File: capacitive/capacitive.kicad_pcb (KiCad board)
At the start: 2 copper layers, 78 x 72 mm, 84 parts, among them J101 UL, J102 UART, J103 SWD, J104 TX_PADS, J105 RX_PAD, J106 POWER, J107 UR, J108 LL, J109 LR, Q101 RU1C002ZPTCL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

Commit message: Move capacitor so it doesn't cover some designators
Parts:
- moved R121 9.40 mm to (139.8, 102.9), turned to 180 degrees
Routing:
- net Net-(C124-Pad2): track 21.2 -> 28.6 mm
- net Net-(C126-Pad2): track 17.1 -> 12.3 mm
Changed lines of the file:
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@@
   )
   (setup
-    (last_trace_width 0.3)
+    (last_trace_width 0.45)
     (user_trace_width 0.2)
     (user_trace_width 0.3)
@@
     (tags "resistor 1206")
     (attr smd)
-    (fp_text reference R117 (at 0.21 9.035 270) (layer F.SilkS)
+    (fp_text reference R117 (at 0.21 7.225 270) (layer F.SilkS)
       (effects (font (size 1 1) (thickness 0.15)))
     )
@@
     (tags "resistor 1206")
     (attr smd)
-    (fp_text reference R127 (at 0.195 10.125 270) (layer F.SilkS)
+    (fp_text reference R127 (at 0.195 8.495 270) (layer F.SilkS)
       (effects (font (size 1 1) (thickness 0.15)))
     )
@@
   )
   (module Resistors_SMD:R_1206_HandSoldering (layer F.Cu)
-    (at 143.51 94.24 270)
+    (at 139.795 102.87 180)
     (descr "Resistor SMD 1206, hand soldering")
     (tags "resistor 1206")
     (attr smd)
-    (fp_text reference R121 (at 0 -1.85 270) (layer F.SilkS)
+    (fp_text reference R121 (at 0 -1.85 180) (layer F.SilkS)
       (effects (font (size 1 1) (thickness 0.15)))
     )
-    (fp_text value "100k 1%" (at 0 1.9 270) (layer F.Fab)
+    (fp_text value "100k 1%" (at 0 1.9 180) (layer F.Fab)
       (effects (font (size 1 1) (thickness 0.15)))
     )
@@
     (fp_line (start 1.6 0.8) (end -1.6 0.8) (layer F.Fab) (width 0.1))
     (fp_line (start -1.6 0.8) (end -1.6 -0.8) (layer F.Fab) (width 0.1))
-    (fp_text user %R (at 0 0 270) (layer F.Fab)
+    (fp_text user %R (at 0 0 180) (layer F.Fab)
       (effects (font (size 0.7 0.7) (thickness 0.105)))
     )
-    (pad 2 smd rect (at 2 0 270) (size 2 1.7) (layers F.Cu F.Paste F.Mask)
+    (pad 2 smd rect (at 2 0 180) (size 2 1.7) (layers F.Cu F.Paste F.Mask)
       (net 37 "Net-(C126-Pad2)"))
-    (pad 1 smd rect (at -2 0 270) (size 2 1.7) (layers F.Cu F.Paste F.Mask)
+    (pad 1 smd rect (at -2 0 180) (size 2 1.7) (layers F.Cu F.Paste F.Mask)
       (net 34 "Net-(C124-Pad2)"))
     (model ${KISYS3DMOD}/Resistors_SMD.3dshapes/R_1206.wrl
@@
   (segment (start 133.18 93.13) (end 132.48 92.43) (width 0.3) (layer B.Cu) (net 34))
   (via (at 132.48 92.43) (size 0.6858) (drill 0.3302) (layers F.Cu B.Cu) (net 34))
-  (segment (start 141.125 92.24) (end 140.41 92.955) (width 0.3) (layer F.Cu) (net 34))
   (segment (start 140.41 92.955) (end 140.41 93.18) (width 0.3) (layer F.Cu) (net 34))
-  (segment (start 143.51 92.24) (end 141.125 92.24) (width 0.3) (layer F.Cu) (net 34))
+  (segment (start 141.795 101.57) (end 141.795 102.87) (width 0.45) (layer F.Cu) (net 34))
+  (segment (start 141.795 93.74) (end 141.795 101.57) (width 0.45) (layer F.Cu) (net 34))
+  (segment (start 141.235 93.18) (end 141.795 93.74) (width 0.45) (layer F.Cu) (net 34))
+  (segment (start 140.41 93.18) (end 141.235 93.18) (width 0.45) (layer F.Cu) (net 34))
   (segment (start 138.05 89.54) (end 138.05 87.69) (width 0.6) (layer F.Cu) (net 35))
   (segment (start 138.05 87.69) (end 138.05 85.695678) (width 0.6) (layer F.Cu) (net 35))
@@
   (segment (start 132.334952 95.69) (end 131.3 95.69) (width 0.3) (layer F.Cu) (net 37))
   (segment (start 132.650254 96.005302) (end 132.334952 95.69) (width 0.3) (layer F.Cu) (net 37))
-  (segment (start 135.312401 99.302401) (end 135.04 99.03) (width 0.3) (layer F.Cu) (net 37))
-  (segment (start 135.04 99.03) (end 134.14 99.03) (width 0.3) (layer F.Cu) (net 37))
-  (segment (start 140.597599 99.302401) (end 135.312401 99.302401) (width 0.3) (layer F.Cu) (net 37))
-  (segment (start 143.51 96.39) (end 140.597599 99.302401) (width 0.3) (layer F.Cu) (net 37))
-  (segment (start 143.51 96.24) (end 143.51 96.39) (width 0.3) (layer F.Cu) (net 37))
+  (segment (start 137.795 101.57) (end 137.795 102.87) (width 0.45) (layer F.Cu) (net 37))
+  (segment (start 135.255 99.03) (end 137.795 101.57) (width 0.45) (layer F.Cu) (net 37))
+  (segment (start 134.14 99.03) (end 135.255 99.03) (width 0.45) (layer F.Cu) (net 37))
   (segment (start 133.945 100.42) (end 134.17 100.42) (width 0.2) (layer F.Cu) (net 38))
   (segment (start 132.83 97.66) (end 132.83 98.16) (width 0.2) (layer F.Cu) (net 38))

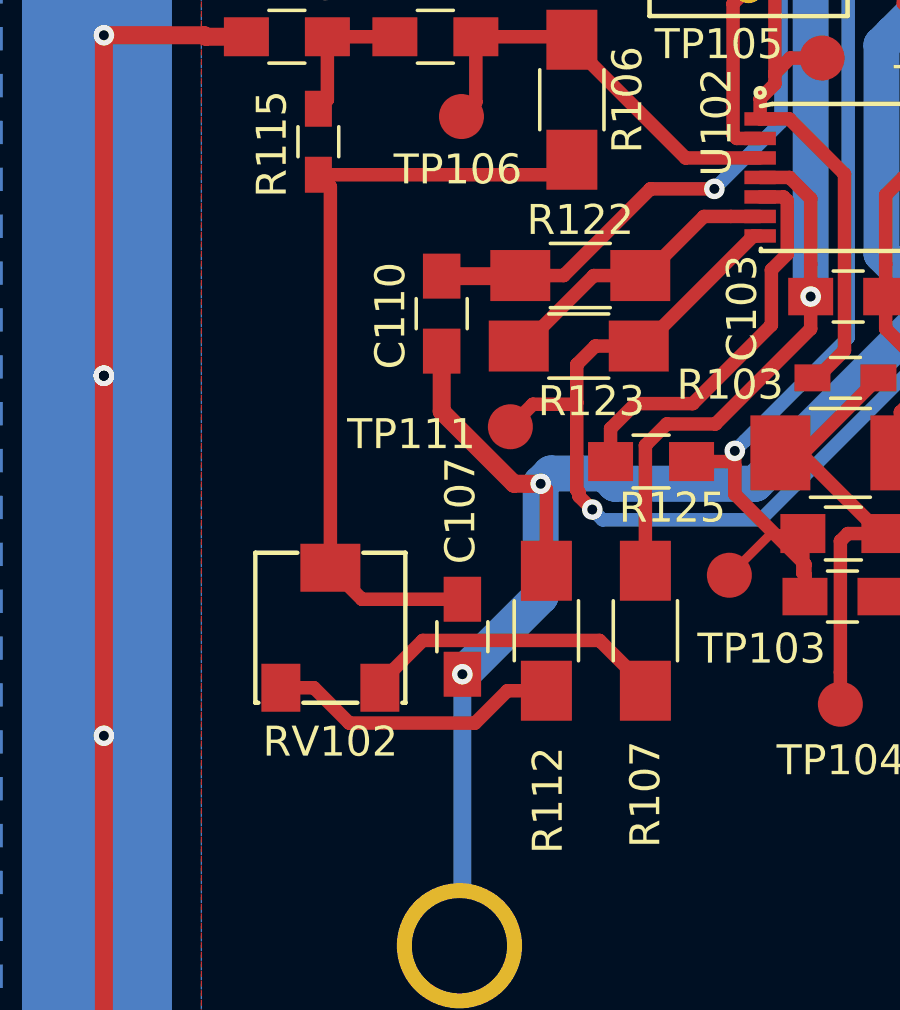
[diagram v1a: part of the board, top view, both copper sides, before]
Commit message: Flip offset pot around to make it more accessible TODO maybe remove offset pot to save cost
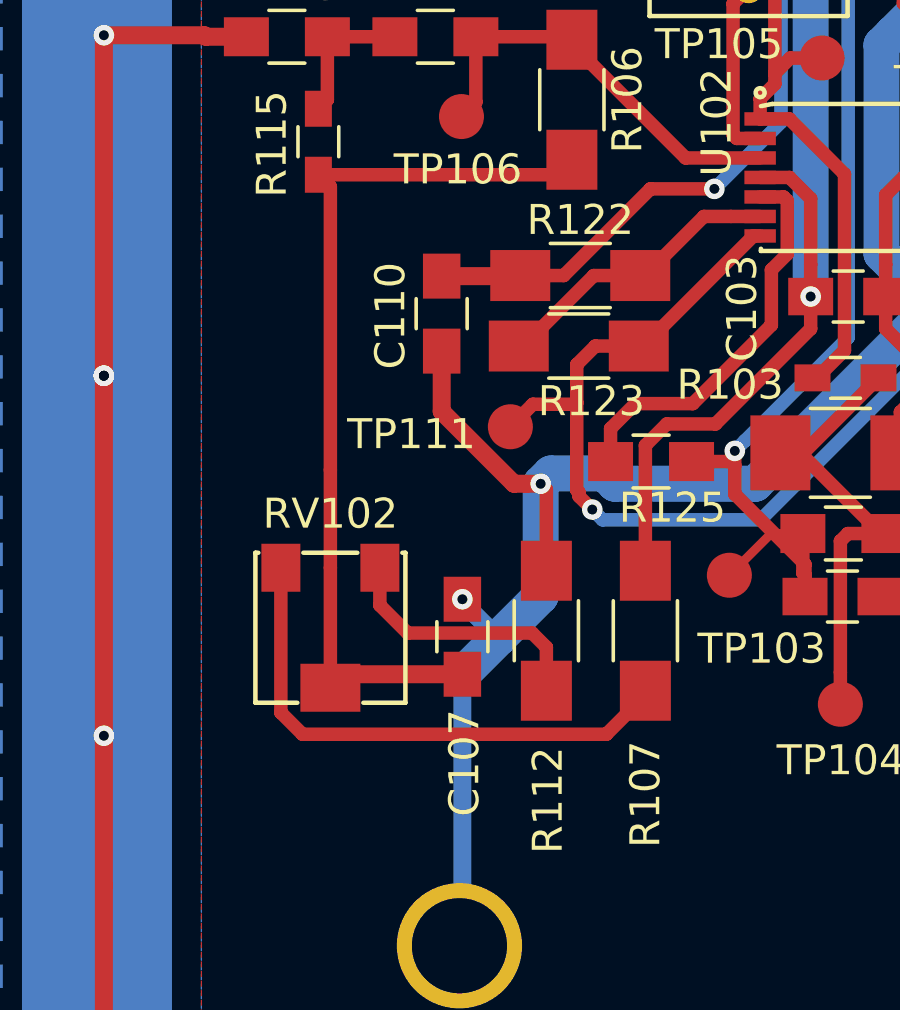
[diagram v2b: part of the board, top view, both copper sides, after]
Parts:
- turned C107 to 90 degrees
- turned RV102 to 180 degrees
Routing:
- net Net-(R107-Pad2): track 10.4 -> 18.1 mm
- net Net-(C107-Pad1): track 26.8 -> 30.5 mm
- net GND: track 430.9 -> 432.7 mm
- net Net-(R112-Pad1): track 9.78 -> 8.83 mm
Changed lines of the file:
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@@
     (thickness 1.6)
     (drawings 9)
-    (tracks 810)
+    (tracks 816)
     (zones 0)
     (modules 84)
@@
   )
   (setup
-    (last_trace_width 0.45)
+    (last_trace_width 0.6)
     (user_trace_width 0.2)
     (user_trace_width 0.3)
@@
   )
   (module capacitive:Bourns-PVG5H (layer F.Cu)
-    (at 110.6 109.4)
-    (fp_text reference RV102 (at 0 3.8) (layer F.SilkS)
+    (at 110.6 109.4 180)
+    (fp_text reference RV102 (at 0 3.8 180) (layer F.SilkS)
       (effects (font (size 1 1) (thickness 0.15)))
     )
-    (fp_text value "5k linear" (at 0 -3.7) (layer F.Fab)
+    (fp_text value "5k linear" (at 0 -3.7 180) (layer F.Fab)
       (effects (font (size 1 1) (thickness 0.15)))
     )
@@
     (fp_line (start -2.5 -2.5) (end -2.5 2.5) (layer F.SilkS) (width 0.15))
     (fp_line (start -1.1 -2.5) (end -2.5 -2.5) (layer F.SilkS) (width 0.15))
-    (pad 2 smd rect (at 0 -2) (size 2 1.6) (layers F.Cu F.Paste F.Mask)
+    (pad 2 smd rect (at 0 -2 180) (size 2 1.6) (layers F.Cu F.Paste F.Mask)
       (net 31 "Net-(C107-Pad1)"))
-    (pad 1 smd rect (at 1.65 2) (size 1.3 1.6) (layers F.Cu F.Paste F.Mask)
+    (pad 1 smd rect (at 1.65 2 180) (size 1.3 1.6) (layers F.Cu F.Paste F.Mask)
       (net 29 "Net-(R107-Pad2)"))
-    (pad 3 smd rect (at -1.65 2) (size 1.3 1.6) (layers F.Cu F.Paste F.Mask)
+    (pad 3 smd rect (at -1.65 2 180) (size 1.3 1.6) (layers F.Cu F.Paste F.Mask)
       (net 30 "Net-(R112-Pad1)"))
   )
@@
   )
   (module Capacitors_SMD:C_0805_HandSoldering (layer F.Cu)
-    (at 115 109.7 270)
+    (at 115 109.7 90)
     (descr "Capacitor SMD 0805, hand soldering")
     (tags "capacitor 0805")
     (attr smd)
-    (fp_text reference C107 (at -4.20624 0.06604 270) (layer F.SilkS)
+    (fp_text reference C107 (at -4.20624 0.06604 90) (layer F.SilkS)
       (effects (font (size 1 1) (thickness 0.15)))
     )
-    (fp_text value "100nF 20%" (at 0 1.75 270) (layer F.Fab)
+    (fp_text value "100nF 20%" (at 0 1.75 90) (layer F.Fab)
       (effects (font (size 1 1) (thickness 0.15)))
     )
-    (fp_text user %R (at 0 -1.75 270) (layer F.Fab)
+    (fp_text user %R (at 0 -1.75 90) (layer F.Fab)
       (effects (font (size 1 1) (thickness 0.15)))
     )
@@
     (fp_line (start 2.25 0.87) (end 2.25 -0.88) (layer F.CrtYd) (width 0.05))
     (fp_line (start 2.25 0.87) (end -2.25 0.87) (layer F.CrtYd) (width 0.05))
-    (pad 1 smd rect (at -1.25 0 270) (size 1.5 1.25) (layers F.Cu F.Paste F.Mask)
+    (pad 1 smd rect (at -1.25 0 90) (size 1.5 1.25) (layers F.Cu F.Paste F.Mask)
       (net 31 "Net-(C107-Pad1)"))
-    (pad 2 smd rect (at 1.25 0 270) (size 1.5 1.25) (layers F.Cu F.Paste F.Mask)
+    (pad 2 smd rect (at 1.25 0 90) (size 1.5 1.25) (layers F.Cu F.Paste F.Mask)
       (net 2 GND))
     (model Capacitors_SMD.3dshapes/C_0805.wrl
@@
   (via (at 130.73 88.21) (size 0.6858) (drill 0.3302) (layers F.Cu B.Cu) (net 2))
   (segment (start 117.61 104.6) (end 117.61 108.34) (width 1.2) (layer B.Cu) (net 2))
-  (segment (start 117.61 108.34) (end 115 110.95) (width 1.2) (layer B.Cu) (net 2))
   (segment (start 129.11 98.36) (end 130.4 98.36) (width 0.6) (layer F.Cu) (net 2))
   (segment (start 130.4 98.36) (end 130.47 98.43) (width 0.6) (layer F.Cu) (net 2))
@@
   (segment (start 130.4 61.125) (end 130.4 61) (width 0.6) (layer F.Cu) (net 2))
   (segment (start 135.95 62.47) (end 137.02 62.47) (width 0.6) (layer F.Cu) (net 2))
-  (via (at 115 110.95) (size 0.6858) (drill 0.3302) (layers F.Cu B.Cu) (net 2))
   (segment (start 117.8 107.5) (end 117.8 104.79) (width 0.45) (layer F.Cu) (net 2))
   (segment (start 117.8 104.79) (end 117.61 104.6) (width 0.45) (layer F.Cu) (net 2))
@@
   (segment (start 118.33 63.05) (end 119.26 63.98) (width 0.6) (layer F.Cu) (net 2))
   (segment (start 119.26 63.98) (end 123.74 63.98) (width 0.6) (layer F.Cu) (net 2))
+  (via (at 115 108.45) (size 0.6858) (drill 0.3302) (layers F.Cu B.Cu) (net 2))
+  (segment (start 115 108.45) (end 115 108.54) (width 0.6) (layer B.Cu) (net 2))
+  (segment (start 117.61 108.34) (end 116.205 109.745) (width 1.2) (layer B.Cu) (net 2))
+  (segment (start 115 108.54) (end 116.205 109.745) (width 0.6) (layer B.Cu) (net 2))
+  (segment (start 116.205 109.745) (end 115 110.95) (width 1.2) (layer B.Cu) (net 2))
   (segment (start 136.28 70.15) (end 134.65 70.15) (width 0.45) (layer F.Cu) (net 3))
   (segment (start 134.65 70.15) (end 132.9 68.4) (width 0.45) (layer F.Cu) (net 3))
@@
   (segment (start 90.649999 68.949999) (end 89.9 68.2) (width 0.3) (layer F.Cu) (net 28))
   (segment (start 121.1 111.5) (end 121.1 111.35) (width 0.45) (layer F.Cu) (net 29))
-  (segment (start 121.1 111.35) (end 119.572599 109.822599) (width 0.45) (layer F.Cu) (net 29))
-  (segment (start 119.572599 109.822599) (end 113.677401 109.822599) (width 0.45) (layer F.Cu) (net 29))
-  (segment (start 113.677401 109.822599) (end 112.25 111.25) (width 0.45) (layer F.Cu) (net 29))
-  (segment (start 112.25 111.25) (end 112.25 111.4) (width 0.45) (layer F.Cu) (net 29))
-  (segment (start 117.8 111.5) (end 116.5 111.5) (width 0.45) (layer F.Cu) (net 30))
-  (segment (start 116.5 111.5) (end 115.422599 112.577401) (width 0.45) (layer F.Cu) (net 30))
-  (segment (start 115.422599 112.577401) (end 111.227401 112.577401) (width 0.45) (layer F.Cu) (net 30))
-  (segment (start 111.227401 112.577401) (end 110.05 111.4) (width 0.45) (layer F.Cu) (net 30))
-  (segment (start 110.05 111.4) (end 108.95 111.4) (width 0.45) (layer F.Cu) (net 30))
+  (segment (start 119.8 112.95) (end 121.1 111.65) (width 0.45) (layer F.Cu) (net 29))
+  (segment (start 109.670678 112.95) (end 119.8 112.95) (width 0.45) (layer F.Cu) (net 29))
+  (segment (start 108.95 112.229322) (end 109.670678 112.95) (width 0.45) (layer F.Cu) (net 29))
+  (segment (start 121.1 111.65) (end 121.1 111.5) (width 0.45) (layer F.Cu) (net 29))
+  (segment (start 108.95 107.4) (end 108.95 112.229322) (width 0.45) (layer F.Cu) (net 29))
+  (segment (start 112.25 108.65) (end 112.25 107.4) (width 0.45) (layer F.Cu) (net 30))
+  (segment (start 117.327401 109.577401) (end 113.177401 109.577401) (width 0.45) (layer F.Cu) (net 30))
+  (segment (start 117.8 110.05) (end 117.327401 109.577401) (width 0.45) (layer F.Cu) (net 30))
+  (segment (start 113.177401 109.577401) (end 112.25 108.65) (width 0.45) (layer F.Cu) (net 30))
+  (segment (start 117.8 111.5) (end 117.8 110.05) (width 0.45) (layer F.Cu) (net 30))
   (segment (start 110.2 94.3) (end 118.15 94.3) (width 0.45) (layer F.Cu) (net 31))
   (segment (start 118.15 94.3) (end 118.65 93.8) (width 0.45) (layer F.Cu) (net 31))
-  (segment (start 110.6 107.4) (end 110.6 94.7) (width 0.45) (layer F.Cu) (net 31))
   (segment (start 110.6 94.7) (end 110.2 94.3) (width 0.45) (layer F.Cu) (net 31))
-  (segment (start 115 108.45) (end 111.65 108.45) (width 0.45) (layer F.Cu) (net 31))
-  (segment (start 111.65 108.45) (end 110.6 107.4) (width 0.45) (layer F.Cu) (net 31))
+  (segment (start 110.6 107.4) (end 110.6 104.14) (width 0.45) (layer F.Cu) (net 31))
+  (segment (start 110.6 104.14) (end 110.6 94.7) (width 0.45) (layer F.Cu) (net 31))
+  (segment (start 110.6 107.4) (end 110.6 111.4) (width 0.45) (layer F.Cu) (net 31))
+  (segment (start 111.05 110.95) (end 110.6 111.4) (width 0.6) (layer F.Cu) (net 31))
+  (segment (start 115 110.95) (end 111.05 110.95) (width 0.6) (layer F.Cu) (net 31))
   (segment (start 123.9 107.65) (end 125.29 106.26) (width 0.3) (layer F.Cu) (net 32))
   (segment (start 125.29 106.26) (end 126.35 106.26) (width 0.3) (layer F.Cu) (net 32))
